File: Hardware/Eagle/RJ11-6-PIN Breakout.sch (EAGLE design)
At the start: 2 parts, among them J1 Molex 22122044, J2 Amphenol MRJR-3460-0F

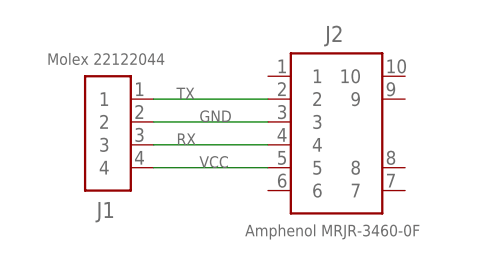
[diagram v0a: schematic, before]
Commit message: Re-pinned the serial connector, changed track widths
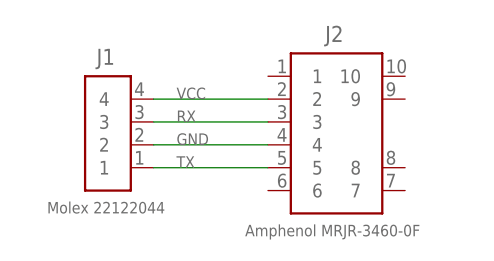
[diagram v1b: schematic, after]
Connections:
- net GND: now also J2.4; no longer J2.3
- net RX: now also J2.3; no longer J2.4
- net TX: now also J2.5; no longer J2.2
- net VCC: now also J2.2; no longer J2.5
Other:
- moved on the sheet: J1
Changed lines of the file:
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@@
 <attribute name="VALUE" x="43.18" y="30.48" size="1.27" layer="96"/>
 </instance>
-<instance part="J1" gate="G$1" x="27.94" y="40.64" smashed="yes" rot="MR0">
-<attribute name="NAME" x="26.67" y="34.29" size="1.778" layer="95" rot="MR180"/>
-<attribute name="VALUE" x="34.29" y="49.53" size="1.27" layer="96" rot="MR0"/>
+<instance part="J1" gate="G$1" x="27.94" y="43.18" smashed="yes" rot="R180">
+<attribute name="NAME" x="26.67" y="49.53" size="1.778" layer="95"/>
+<attribute name="VALUE" x="34.29" y="34.29" size="1.27" layer="96" rot="R180"/>
 </instance>
 </instances>
@@
 </busses>
 <nets>
-<net name="TX" class="0">
+<net name="VCC" class="0">
 <segment>
+<pinref part="J1" gate="G$1" pin="4"/>
 <pinref part="J2" gate="G$1" pin="2"/>
+<wire x1="33.02" y1="45.72" x2="45.72" y2="45.72" width="0.1524" layer="91"/>
 <label x="35.56" y="45.72" size="1.27" layer="95"/>
-<pinref part="J1" gate="G$1" pin="1"/>
-<wire x1="33.02" y1="45.72" x2="45.72" y2="45.72" width="0.1524" layer="91"/>
+</segment>
+</net>
+<net name="RX" class="0">
+<segment>
+<pinref part="J2" gate="G$1" pin="3"/>
+<pinref part="J1" gate="G$1" pin="3"/>
+<wire x1="45.72" y1="43.18" x2="33.02" y2="43.18" width="0.1524" layer="91"/>
+<label x="35.56" y="43.18" size="1.27" layer="95"/>
 </segment>
 </net>
 <net name="GND" class="0">
 <segment>
-<pinref part="J2" gate="G$1" pin="3"/>
-<label x="38.1" y="43.18" size="1.27" layer="95"/>
 <pinref part="J1" gate="G$1" pin="2"/>
-<wire x1="33.02" y1="43.18" x2="45.72" y2="43.18" width="0.1524" layer="91"/>
+<pinref part="J2" gate="G$1" pin="4"/>
+<wire x1="33.02" y1="40.64" x2="45.72" y2="40.64" width="0.1524" layer="91"/>
+<label x="35.56" y="40.64" size="1.27" layer="95"/>
 </segment>
 </net>
-<net name="RX" class="0">
+<net name="TX" class="0">
 <segment>
-<pinref part="J2" gate="G$1" pin="4"/>
-<label x="35.56" y="40.64" size="1.27" layer="95"/>
-<wire x1="33.02" y1="40.64" x2="45.72" y2="40.64" width="0.1524" layer="91"/>
-<pinref part="J1" gate="G$1" pin="3"/>
+<pinref part="J2" gate="G$1" pin="5"/>
+<pinref part="J1" gate="G$1" pin="1"/>
+<wire x1="45.72" y1="38.1" x2="33.02" y2="38.1" width="0.1524" layer="91"/>
+<label x="35.56" y="38.1" size="1.27" layer="95"/>
 </segment>
 </net>
-<net name="VCC" class="0">
-<segment>
-<pinref part="J2" gate="G$1" pin="5"/>
-<label x="38.1" y="38.1" size="1.27" layer="95"/>
-<wire x1="33.02" y1="38.1" x2="45.72" y2="38.1" width="0.1524" layer="91"/>
-<pinref part="J1" gate="G$1" pin="4"/>
-</segment>
-</net>
